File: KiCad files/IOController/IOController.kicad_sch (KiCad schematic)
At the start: 19 parts, among them J1 AVR-ISP-6, J3 XT60 Horizontal Socket, J6 XT60 Horizontal Socket, Q1 BSS138, SW1 RotaryEncoder_Switch, SW2 SW_Push, U1 ATtiny85-20P, U3 LP2985-1.8, U4 LP2985-5.0

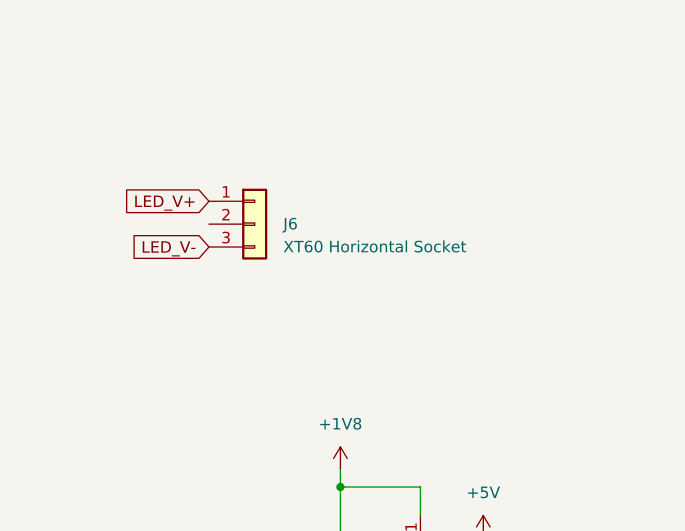
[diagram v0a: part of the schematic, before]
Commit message: updated LED board to use new LEDs
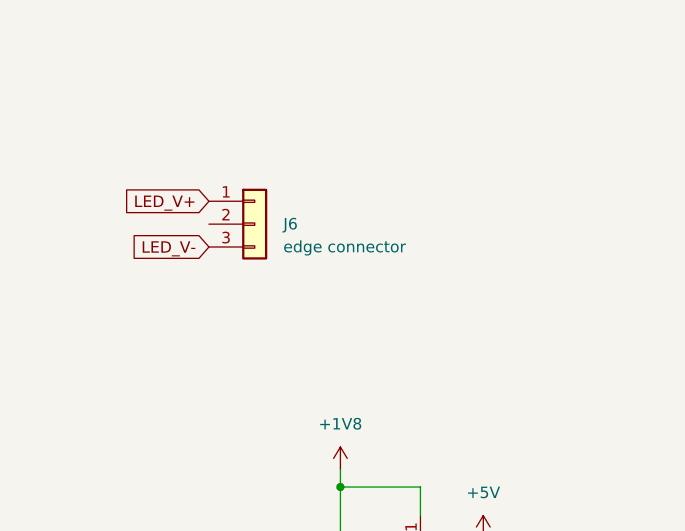
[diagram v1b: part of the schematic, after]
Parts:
- J6: value XT60 Horizontal Socket -> edge connector
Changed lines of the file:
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@@
       (effects (font (size 1.27 1.27)) (justify left))
     )
-    (property "Value" "XT60 Horizontal Socket" (at 172.085 39.37 0)
+    (property "Value" "edge connector" (at 172.085 39.37 0)
       (effects (font (size 1.27 1.27)) (justify left))
     )

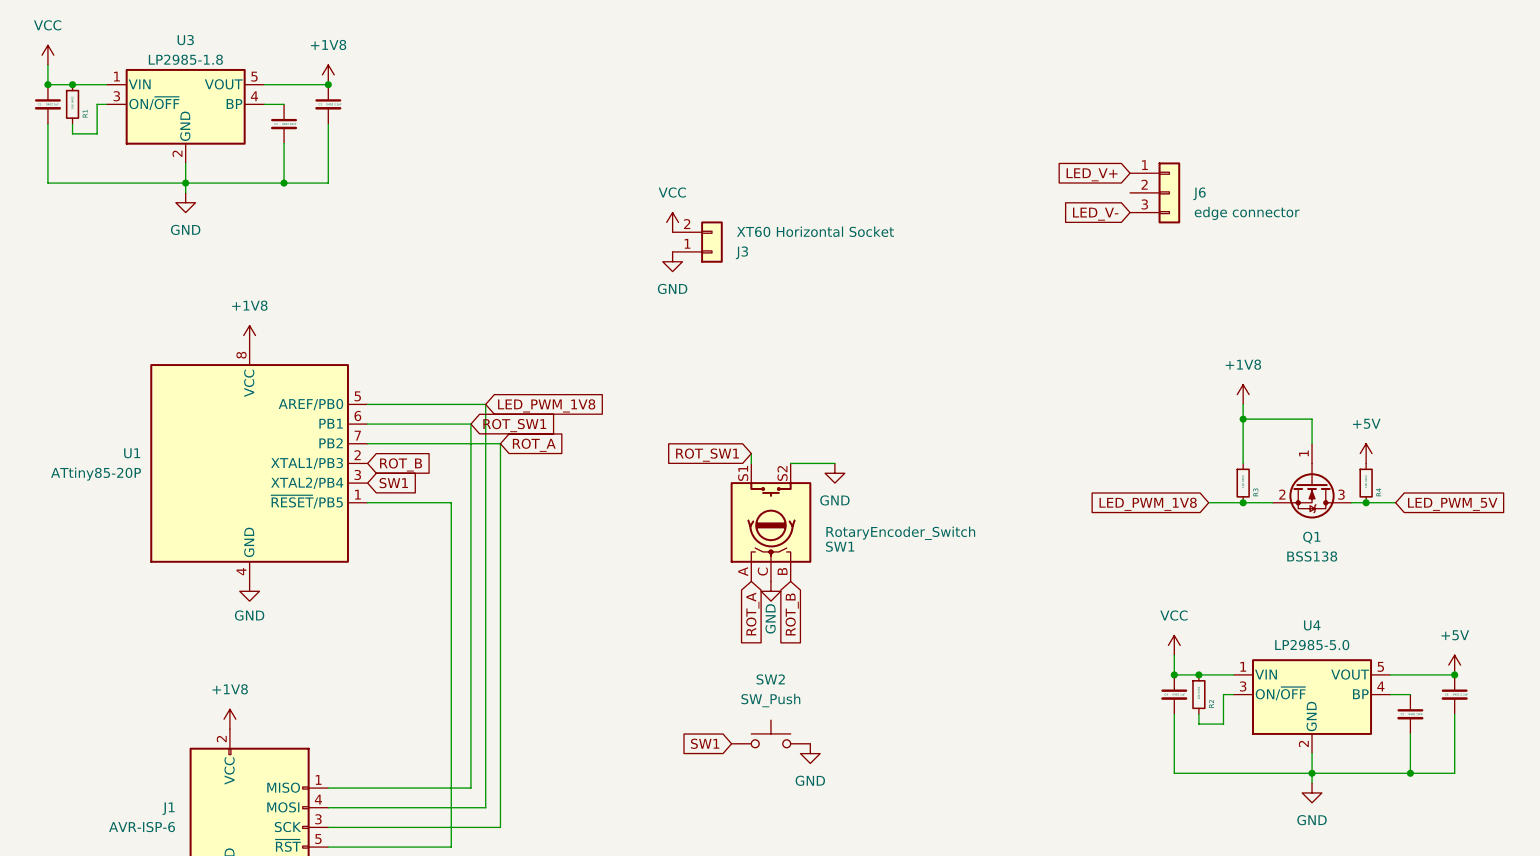
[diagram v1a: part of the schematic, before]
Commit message: started re-work of led driver circuit on IO board
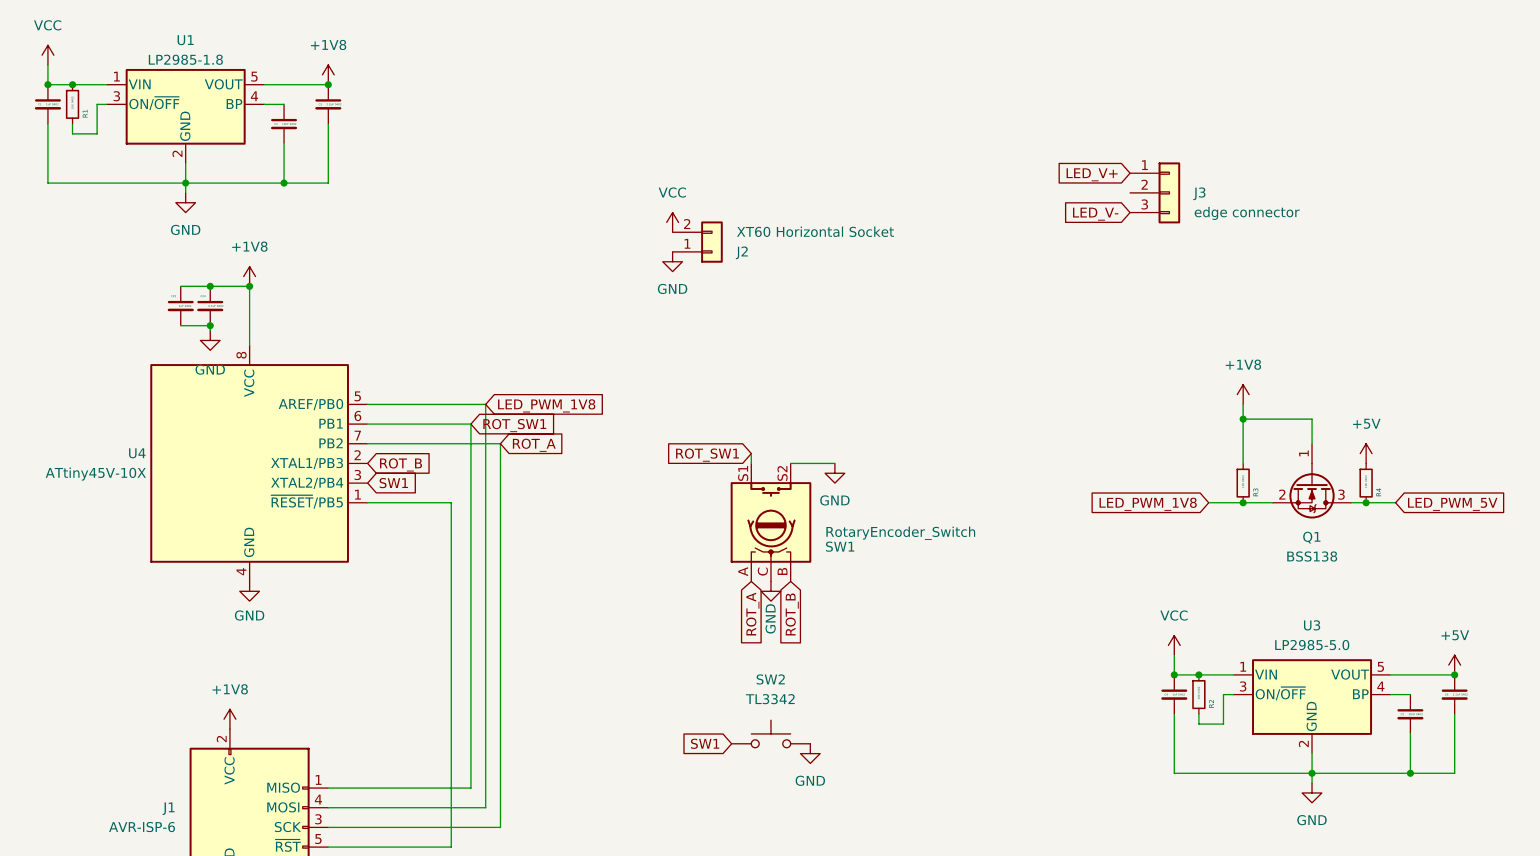
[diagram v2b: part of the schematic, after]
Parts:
- removed U1: ATtiny85-20P, Package_DIP:DIP-8_W7.62mm, symbol MCU_Microchip_ATtiny:ATtiny85-20P
- added C24: 0.1uF 0402, Capacitor_SMD:C_0402_1005Metric, symbol Device:C_Small
- added C25: 1uF 0402, Capacitor_SMD:C_0402_1005Metric, symbol Device:C_Small
- added U4: ATtiny45V-10X, Package_SO:TSSOP-8_4.4x3mm_P0.65mm, symbol MCU_Microchip_ATtiny:ATtiny45V-10X
- C1, C4: value 0402 1uF -> 1uF 0402
- C2, C5: value 0402 10nF -> 10nF 0402
- C3, C6: value 0402 2.2uF -> 2.2uF 0402
- J3: renamed from J6; footprint Connector_PinHeader_2.54mm:PinHeader_1x03_P2.54mm_Vertical -> EnvExtras:CardEdge1x03
- SW2: value SW_Push -> TL3342; footprint Button_Switch_SMD:SW_SPST_B3U-1000P -> Button_Switch_SMD:SW_SPST_TL3342
- renumbered J3 to J2, U3 to U1, U4 to U3
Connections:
- net +1V8: now also C24.1, C25.1, U4.8 (VCC)
- net GND: now also C24.2, C25.2, U4.4 (GND)
- net LED_PWM_1V8: now also U4.5 (AREF/PB0)
- net ROT_A: now also U4.7 (PB2)
- net ROT_B: now also U4.2 (XTAL1/PB3)
- net ROT_SW1: now also U4.6 (PB1)
- net SW1: now also U4.3 (XTAL2/PB4)
- net at J1.5 (~{RST}): now also U4.1 (~{RESET}/PB5)

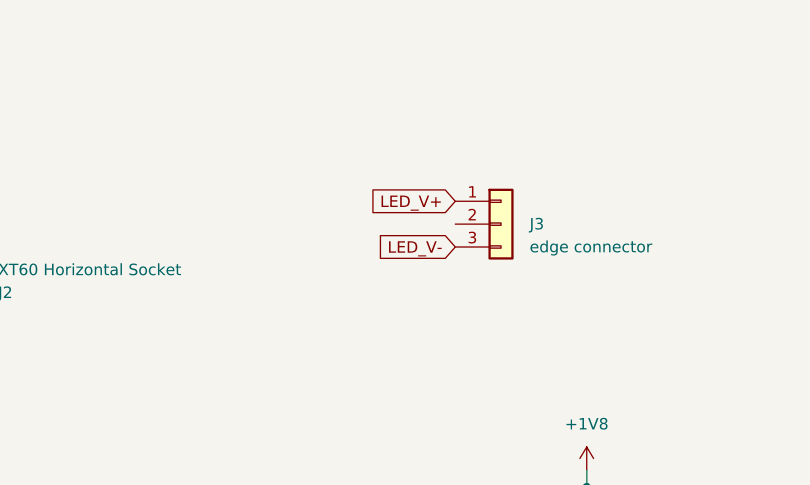
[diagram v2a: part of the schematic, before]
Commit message: completed circuit, could be laid out better
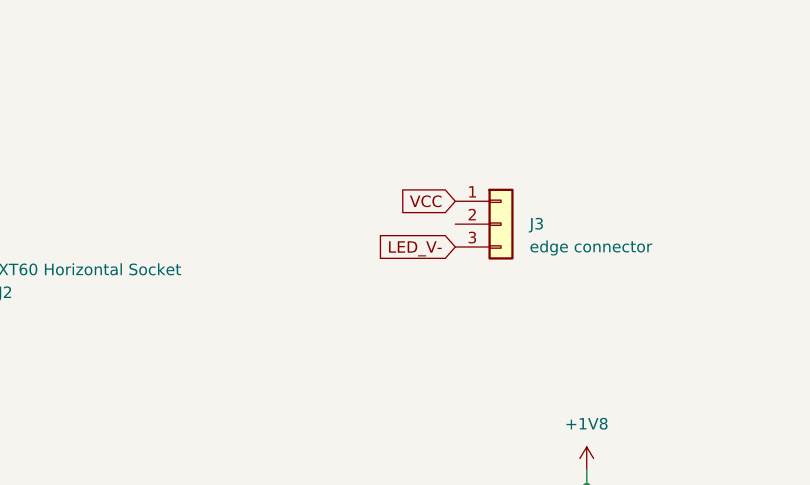
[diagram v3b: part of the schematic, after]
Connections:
- net LED_V+ is gone; now on net VCC: J3.1 (Pin_1)
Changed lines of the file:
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@@
     )
   )
-  (global_label "LED_V+" (shape input) (at 163.83 34.29 180) (fields_autoplaced)
+  (global_label "VCC" (shape input) (at 163.83 34.29 180) (fields_autoplaced)
     (effects (font (size 1.27 1.27)) (justify right))
-    (property "Intersheetrefs" "${INTERSHEET_REFS}" (at 153.7691 34.29 0)
+    (property "Intersheetrefs" "${INTERSHEET_REFS}" (at 157.2162 34.29 0)
       (effects (font (size 1.27 1.27)) (justify right) hide)
     )

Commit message: updated small changes
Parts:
- J1: footprint Connector_PinHeader_1.00mm:PinHeader_2x03_P1.00mm_Vertical -> Connector_PinHeader_2.54mm:PinHeader_2x03_P2.54mm_Vertical
- SW2: value TL3342 -> B3U; footprint Button_Switch_SMD:SW_SPST_TL3342 -> Button_Switch_SMD:SW_SPST_B3U-1000P-B
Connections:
- net ROT_A: now also U4.3 (XTAL2/PB4); no longer J1.3 (SCK), U4.7 (PB2)
- net SW1: now also J1.3 (SCK), U4.7 (PB2); no longer U4.3 (XTAL2/PB4)
- net VCC: no longer J3.1 (Pin_1)
- new net LED V+: J3.1 (Pin_1)
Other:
- title: (none) -> IO, input and PSU
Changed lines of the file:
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@@
 (kicad_sch (version 20230121) (generator eeschema)
   (paper "A4")
+  (title_block
+    (title "IO, input and PSU")
+  )
   (junction (at 60.325 22.86) (diameter 0) (color 0 0 0 0)
   )
@@
     (stroke (width 0) (type default))
   )
-  (global_label "SW1" (shape input) (at 65.405 74.295 0) (fields_autoplaced)
+  (global_label "SW1" (shape input) (at 82.55 69.215 0) (fields_autoplaced)
     (effects (font (size 1.27 1.27)) (justify left))
-    (property "Intersheetrefs" "${INTERSHEET_REFS}" (at 72.2606 74.295 0)
+    (property "Intersheetrefs" "${INTERSHEET_REFS}" (at 89.4056 69.215 0)
       (effects (font (size 1.27 1.27)) (justify left) hide)
     )
   )
-  (global_label "ROT_A" (shape input) (at 82.55 69.215 0) (fields_autoplaced)
+  (global_label "ROT_A" (shape input) (at 65.405 74.295 0) (fields_autoplaced)
     (effects (font (size 1.27 1.27)) (justify left))
-    (property "Intersheetrefs" "${INTERSHEET_REFS}" (at 91.1595 69.215 0)
+    (property "Intersheetrefs" "${INTERSHEET_REFS}" (at 74.0145 74.295 0)
       (effects (font (size 1.27 1.27)) (justify left) hide)
     )
@@
     )
   )
-  (global_label "VCC" (shape input) (at 163.83 34.29 180) (fields_autoplaced)
+  (global_label "LED V+" (shape input) (at 163.83 34.29 180) (fields_autoplaced)
     (effects (font (size 1.27 1.27)) (justify right))
-    (property "Intersheetrefs" "${INTERSHEET_REFS}" (at 157.2162 34.29 0)
+    (property "Intersheetrefs" "${INTERSHEET_REFS}" (at 153.7691 34.29 0)
       (effects (font (size 1.27 1.27)) (justify right) hide)
     )
@@
       (effects (font (size 1.27 1.27)))
     )
-    (property "Value" "TL3342" (at 117.475 102.235 0)
-      (effects (font (size 1.27 1.27)))
-    )
-    (property "Footprint" "Button_Switch_SMD:SW_SPST_TL3342" (at 117.475 102.87 0)
+    (property "Value" "B3U" (at 117.475 102.235 0)
+      (effects (font (size 1.27 1.27)))
+    )
+    (property "Footprint" "Button_Switch_SMD:SW_SPST_B3U-1000P-B" (at 117.475 102.87 0)
       (effects (font (size 1.27 1.27)) hide)
     )
@@
       (effects (font (size 1.27 1.27)) (justify right))
     )
-    (property "Footprint" "Connector_PinHeader_1.00mm:PinHeader_2x03_P1.00mm_Vertical" (at 43.815 117.475 90)
-      (effects (font (size 1.27 1.27)) hide)
-    )
+    (property "Footprint" "Connector_PinHeader_2.54mm:PinHeader_2x03_P2.54mm_Vertical" (at 43.815 117.475 90)
+      (effects (font (size 1.27 1.27)) hide)
+    )

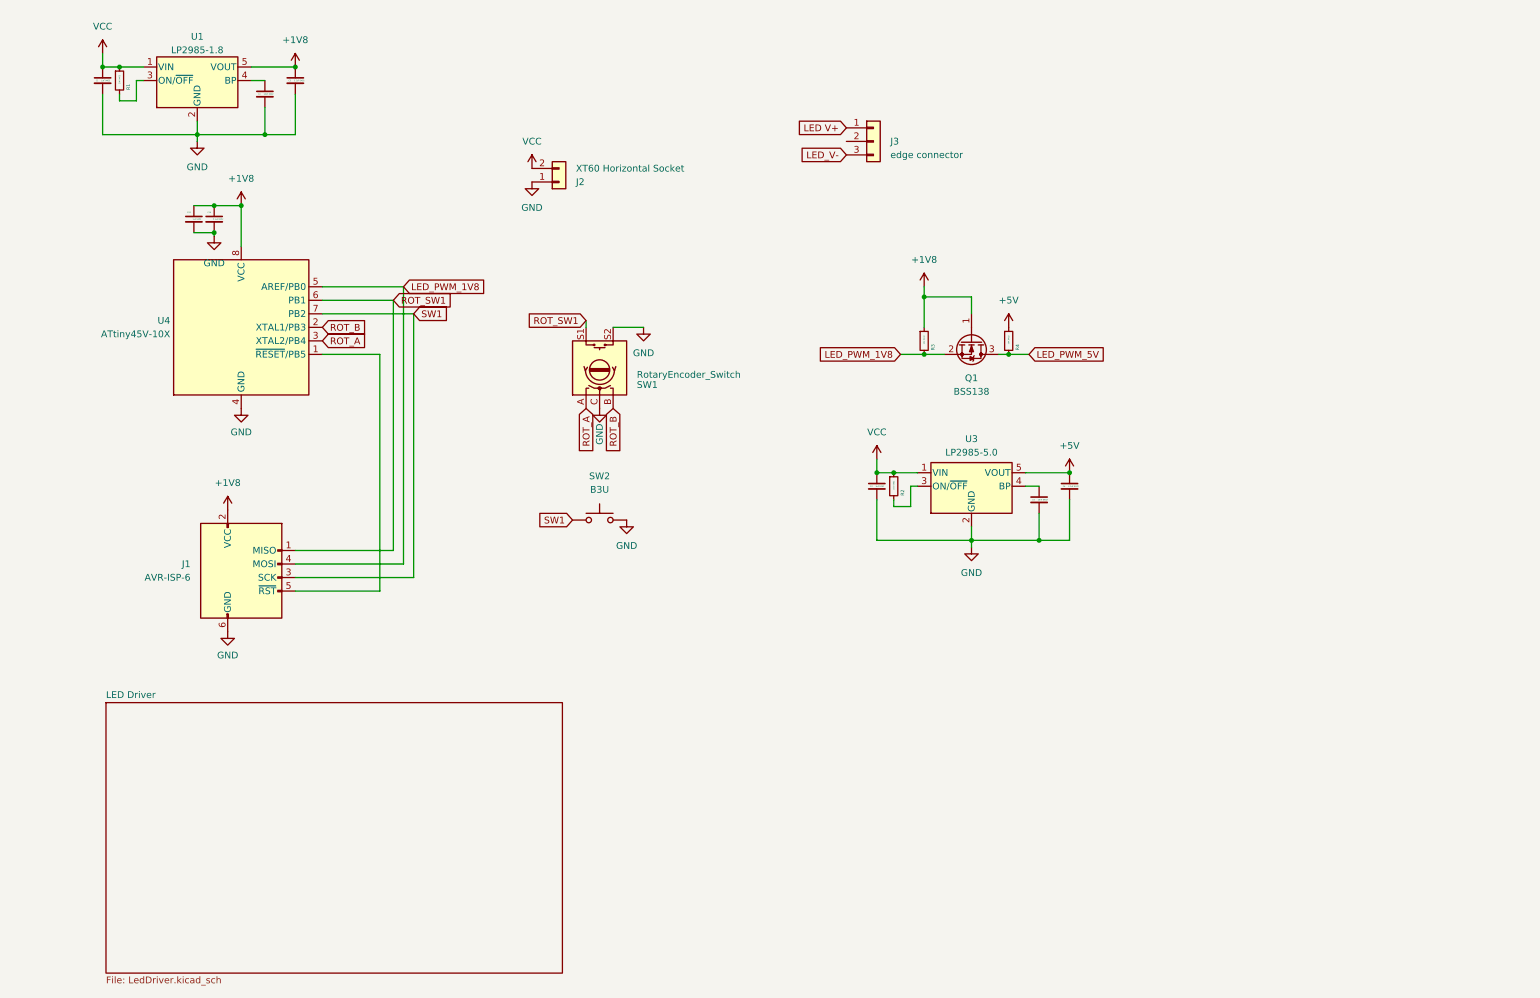
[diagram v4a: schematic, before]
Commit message: re-organised some files, started work on implementing 100W and 240W EPR versions of the charge board
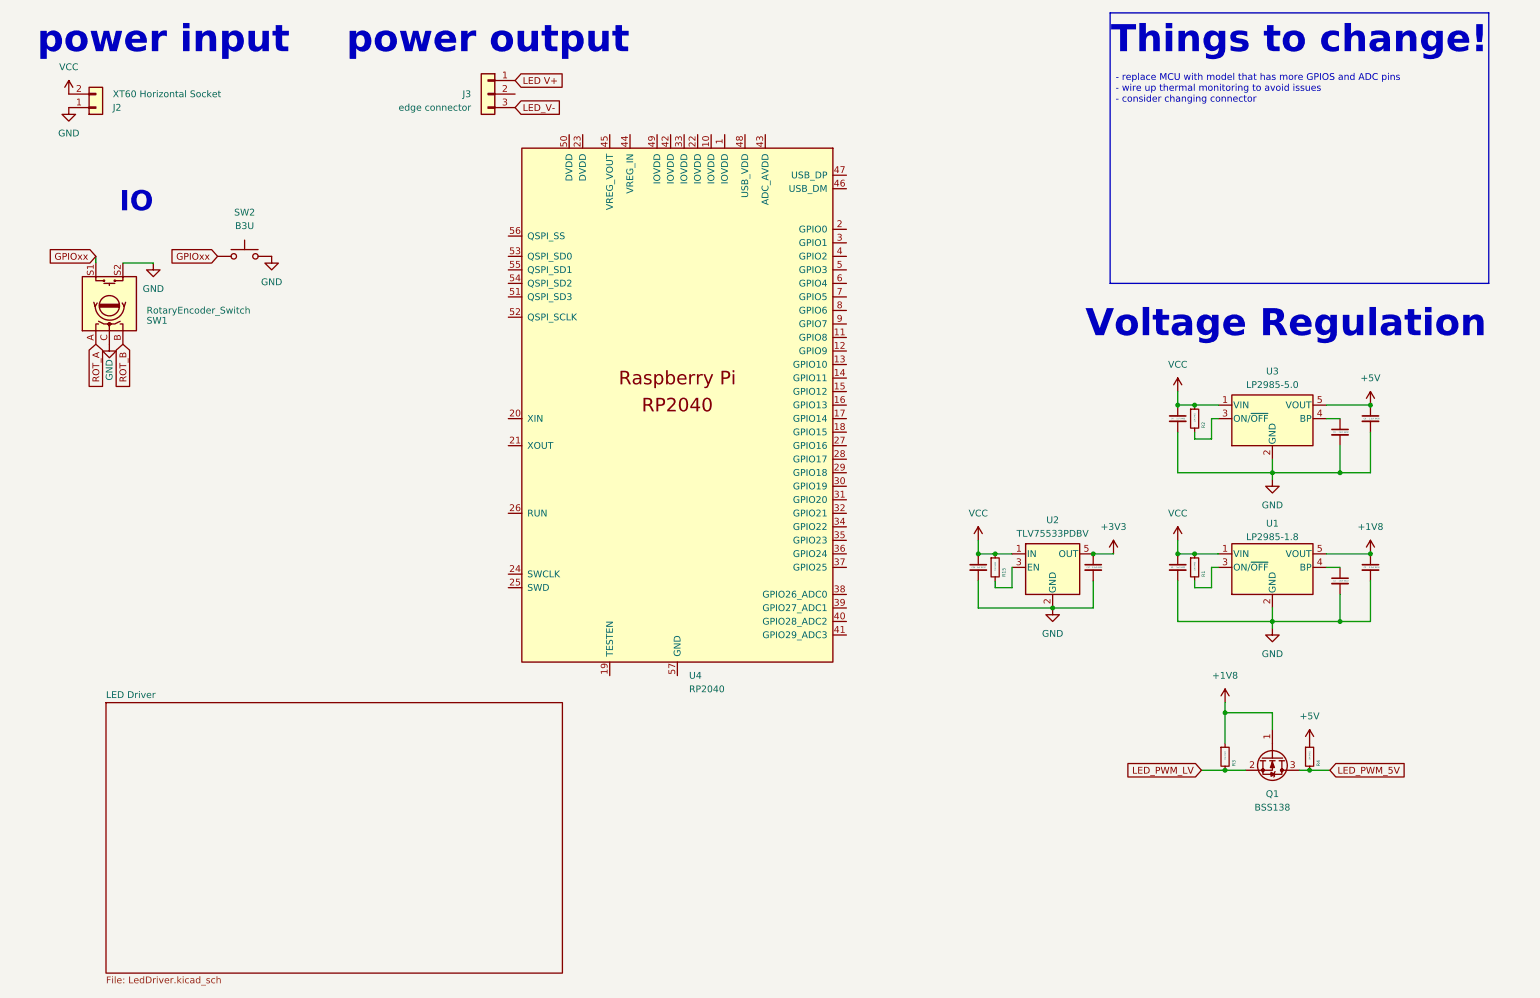
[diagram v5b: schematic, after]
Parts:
- removed C24: 0.1uF 0402, Capacitor_SMD:C_0402_1005Metric, symbol Device:C_Small
- removed C25: 1uF 0402, Capacitor_SMD:C_0402_1005Metric, symbol Device:C_Small
- removed J1: AVR-ISP-6, Connector_PinHeader_2.54mm:PinHeader_2x03_P2.54mm_Vertical, symbol Connector:AVR-ISP-6
- removed U4: ATtiny45V-10X, Package_SO:TSSOP-8_4.4x3mm_P0.65mm, symbol MCU_Microchip_ATtiny:ATtiny45V-10X
- added C26: 1uF 0402, Capacitor_SMD:C_0402_1005Metric, symbol Device:C_Small
- added C27: 2.2uF 0402, Capacitor_SMD:C_0402_1005Metric, symbol Device:C_Small
- added R15: 10K 0402, Resistor_SMD:R_0402_1005Metric, symbol Device:R_Small
- added U2: TLV75533PDBV, Package_TO_SOT_SMD:SOT-23-5, symbol Regulator_Linear:TLV75533PDBV
- added U4: RP2040, RP2040_minimal_r2:RP2040-QFN-56, symbol MCU_RaspberryPi_RP2040:RP2040
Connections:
- net SW1 is gone; now on net GPIOxx: SW2.1
- net GND: now also C26.2, C27.2, U2.2 (GND)
- net VCC: now also C26.1, R15.1, U2.1 (IN)
- net LED_PWM_1V8 renamed LED_PWM_LV
- net ROT_SW1 renamed GPIOxx
- new net: R15.2, U2.3 (EN)
- new net +3V3: C27.1, U2.5 (OUT)
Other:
- note added: "IO"
- note added: "Things to change!"
- note added: "Voltage Regulation"
- note added: "power input"
- note added: "power output"
- moved on the sheet: C1, C2, C3, C4, C5, C6, J2, J3, Q1, R1, R2, R3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
